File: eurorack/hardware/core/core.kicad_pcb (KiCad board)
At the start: 2 copper layers, 19.3 x 67.9 mm, 48 parts, among them J1 ConnNW, J2 ConnSW, J3 ConnNE, J4 ConnSE, J5 Power, J6 SWD, SW1 Reset, SW2 Boot0, U1 STM32F427VGT6, U2 TLV320AIC23BPW, U3 LM1117F-3.3, U4 LM4040C10IDBZR, Y1 Crystal

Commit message: Wire up power section
Signed-off-by: Petr Horacek <hrck@protonmail.com>
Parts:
- moved C4 27.0 mm to (169.0, 68.7), turned to 270 degrees
- moved Y1 24.6 mm to (164.4, 68.0)
- moved C1 21.0 mm to (159.4, 67.2), turned to 180 degrees
- moved C2 2.93 mm to (168.2, 46.2)
- moved C18 1.33 mm to (159.7, 72.7)
- moved C19 1.33 mm to (168.4, 72.4)
- moved C22 1.33 mm to (159.7, 80.3)
- moved C23 1.33 mm to (159.7, 76.3)
- moved R5 1.33 mm to (168.4, 76.2)
- moved R6 1.33 mm to (168.5, 74.3)
- moved U2 1.33 mm to (164.1, 76.5)
- moved R1 0.74 mm to (162.9, 47.1), turned to 180 degrees
- moved C16 0.42 mm to (165.6, 47.2)
- moved C3 0.41 mm to (159.4, 65.9)
- moved C10 0.32 mm to (169.1, 65.7)
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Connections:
- J1 pad 1: Net-(J1-Pad1) -> GND
- J1 pad 2: Net-(J1-Pad2) -> VCC
- J1 pad 3: Net-(J1-Pad3) -> VEE
- J1 pad 4: Net-(J1-Pad4) -> -10V
- J1 pad 5: Net-(J1-Pad5) -> +3V3
- J1 pad 6: Net-(J1-Pad6) -> +3.3VA
- J3 pad 1: Net-(J3-Pad1) -> GND
- J3 pad 2: Net-(J3-Pad2) -> VCC
- J3 pad 3: Net-(J3-Pad3) -> VEE
- J3 pad 4: Net-(J3-Pad4) -> -10V
- J3 pad 5: Net-(J3-Pad5) -> +3V3
- J3 pad 6: Net-(J3-Pad6) -> +3.3VA
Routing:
- net GND: track 0.00 -> 46.1 mm
- net +3V3: track 0.00 -> 32.0 mm
- net -10V: track 0.00 -> 29.8 mm
- net VEE: track 0.00 -> 26.4 mm
- net VCC: track 0.00 -> 23.9 mm
- net +3.3VA: track 0.00 -> 19.7 mm
- net Net-(C5-Pad1): track 0.00 -> 6.13 mm
- net Net-(FB1-Pad1): track 0.00 -> 5.69 mm
- net Net-(FB2-Pad1): track 0.00 -> 5.69 mm
- added copper zone on In1.Cu, net GND
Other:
- copper layers 2 -> 4
- board text added: "DSP"
- board text added: "Power"

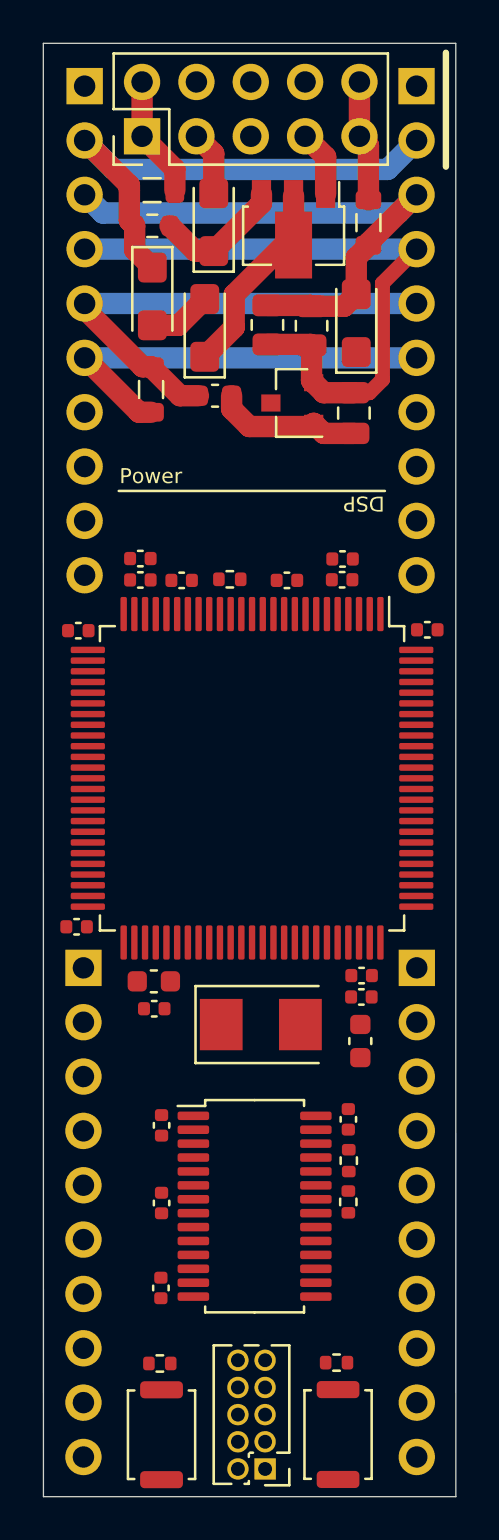
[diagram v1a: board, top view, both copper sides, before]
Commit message: Wire up DAC
Signed-off-by: Petr Horacek <hrck@protonmail.com>
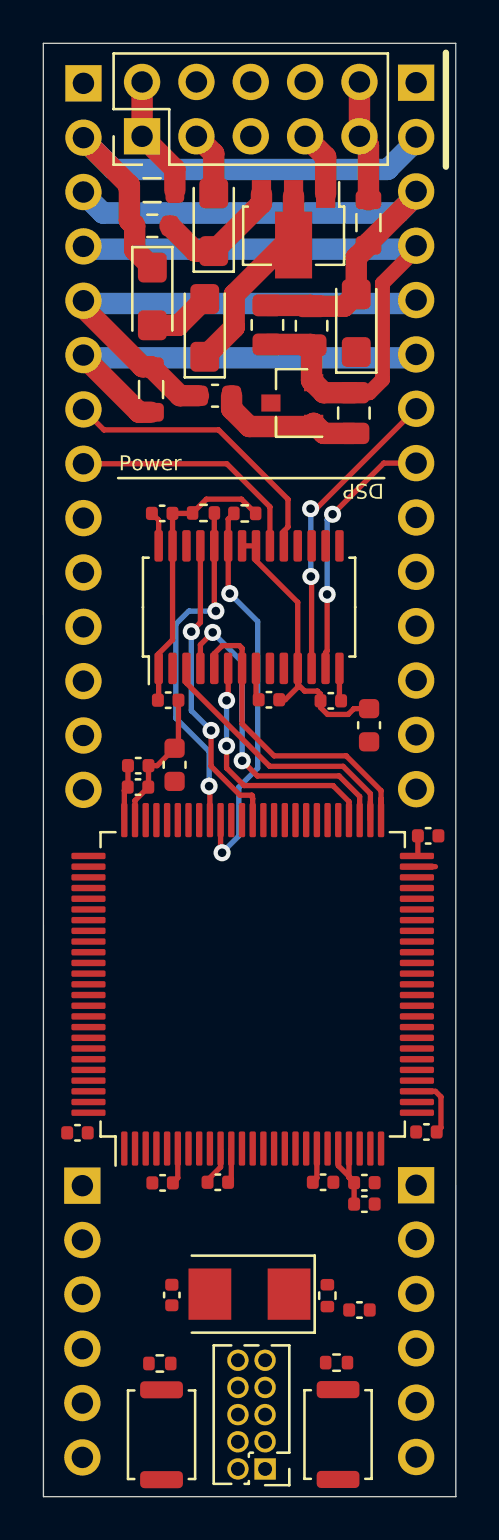
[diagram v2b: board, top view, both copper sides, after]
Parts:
- J1, J3: footprint Connector_PinHeader_2.54mm:PinHeader_1x10_P2.54mm_Vertical -> Connector_PinHeader_2.54mm:PinHeader_1x14_P2.54mm_Vertical
- J2, J4: footprint Connector_PinHeader_2.54mm:PinHeader_1x10_P2.54mm_Vertical -> Connector_PinHeader_2.54mm:PinHeader_1x06_P2.54mm_Vertical
- moved C2 35.3 mm to (160.2, 80.6), turned to 270 degrees
- moved R1 33.8 mm to (167.5, 80.6), turned to 90 degrees
- moved R5 32.5 mm to (163.6, 44.1), turned to 180 degrees
- moved C21 31.9 mm to (169.2, 76.3), turned to 0 degrees
- moved R6 31.0 mm to (161.7, 44.0), turned to 0 degrees
- moved C20 30.1 mm to (169.2, 75.3), turned to 0 degrees
- moved C19 29.6 mm to (159.8, 44.1), turned to 180 degrees
- moved C17 29.4 mm to (159.8, 75.4), turned to 180 degrees
- moved C15 28.9 mm to (167.3, 75.3), turned to 0 degrees
- moved C13 28.6 mm to (155.8, 73.0), turned to 180 degrees
- moved C22 28.6 mm to (167.6, 52.8), turned to 180 degrees
- moved C14 28.5 mm to (172.1, 73.0), turned to 180 degrees
- moved C16 28.3 mm to (162.3, 75.3), turned to 180 degrees
- moved U2 28.0 mm to (163.8, 48.5), turned to 90 degrees
- moved C23 24.0 mm to (164.7, 52.8), turned to 0 degrees
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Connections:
- J1 pad 7: Net-(J1-Pad7) -> RIN
- J1 pad 8: Net-(J1-Pad8) -> LIN
- J3 pad 7: Net-(J3-Pad7) -> LOUT
- J3 pad 8: Net-(J3-Pad8) -> ROUT
- U2 pad 12: Net-(U2-Pad12) -> LOUT
- U2 pad 13: Net-(U2-Pad13) -> ROUT
- U2 pad 19: Net-(U2-Pad19) -> RIN
- U2 pad 20: Net-(U2-Pad20) -> LIN
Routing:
- net +3V3: track 32.0 -> 57.1 mm
- net GND: track 46.1 -> 70.6 mm
- net I2C_SDA: track 0.00 -> 18.8 mm, vias 0 -> 2
- net I2C_SCL: track 0.00 -> 16.6 mm, vias 0 -> 2
- net I2S_WS: track 0.00 -> 15.9 mm
- net I2S_DIN: track 0.00 -> 15.8 mm, vias 0 -> 2
- net I2S_MCK: track 0.00 -> 14.5 mm, vias 0 -> 2
- net LOUT: track 0.00 -> 14.4 mm, vias 0 -> 2
- net RIN: track 0.00 -> 13.6 mm
- net I2S_CK: track 0.00 -> 13.5 mm
- net ROUT: track 0.00 -> 12.2 mm, vias 0 -> 2
- net I2S_DOUT: track 0.00 -> 11.9 mm, vias 0 -> 2
- net LIN: track 0.00 -> 11.4 mm
- net +3.3VA: track 19.7 -> 27.3 mm
- net Net-(C3-Pad1): track 0.00 -> 0.87 mm

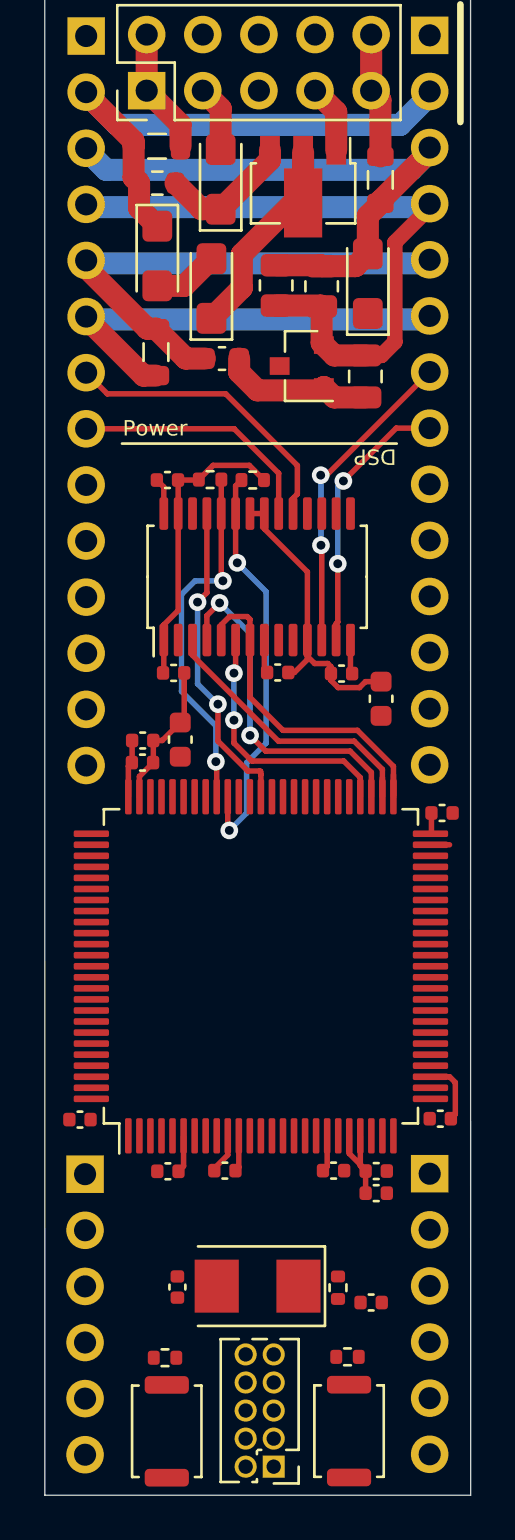
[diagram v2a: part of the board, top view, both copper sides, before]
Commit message: Wire up all pins
Signed-off-by: Petr Horacek <hrck@protonmail.com>
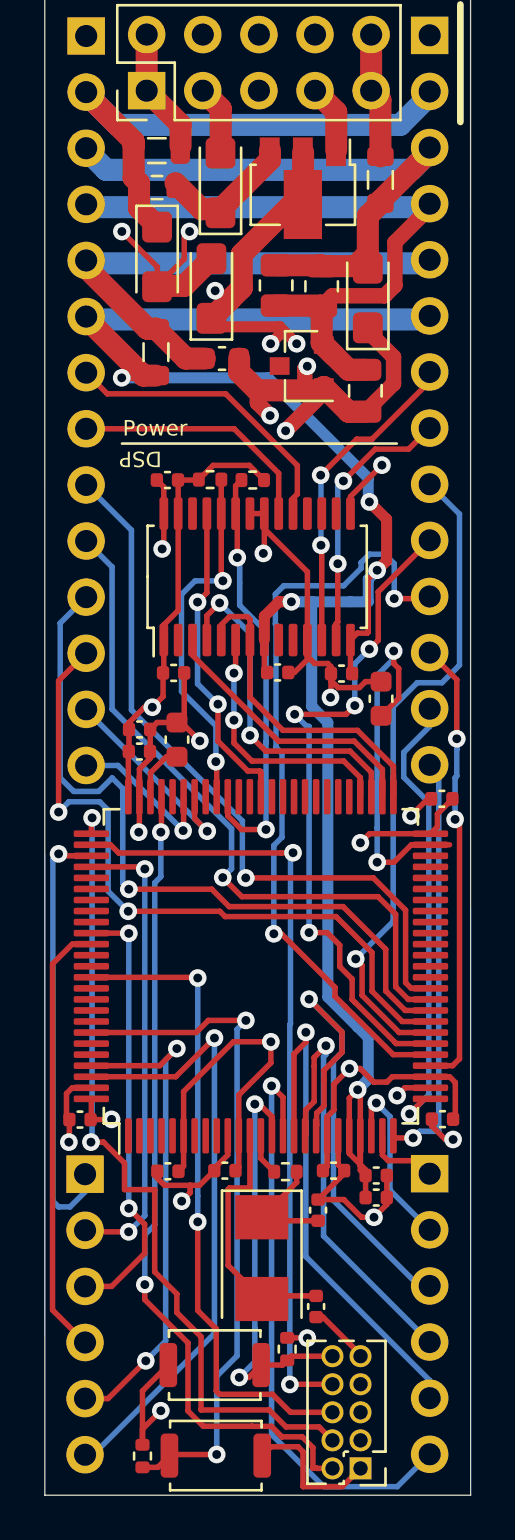
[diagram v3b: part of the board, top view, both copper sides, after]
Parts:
- moved SW1 6.78 mm to (161.9, 84.1), turned to 0 degrees
- moved C2 6.34 mm to (166.5, 81.5)
- moved R1 5.76 mm to (165.1, 75.4), turned to 0 degrees
- moved C1 4.82 mm to (166.6, 77.1), turned to 90 degrees
- moved R3 4.57 mm to (158.6, 88.2), turned to 90 degrees
- moved J6 3.93 mm to (168.5, 88.8)
- moved R2 2.75 mm to (165.2, 83.4), turned to 270 degrees
- moved SW2 2.48 mm to (161.9, 88.2), turned to 0 degrees
- moved Y1 1.28 mm to (164.0, 79.3), turned to 270 degrees
- moved C24 0.65 mm to (168.7, 40.0)
- moved C9 0.65 mm to (168.8, 35.8)
- moved C12 0.64 mm to (172.2, 58.5), turned to 180 degrees
- moved C10 0.52 mm to (158.5, 56.4)
- moved C11 0.52 mm to (158.5, 55.4)
- moved FB1 0.20 mm to (159.3, 29.2)
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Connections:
- J1 pad 10: Net-(J1-Pad10) -> PIN2
- J1 pad 11: Net-(J1-Pad11) -> PIN3
- J1 pad 12: Net-(J1-Pad12) -> PIN4
- J1 pad 13: Net-(J1-Pad13) -> PIN5
- J1 pad 14: Net-(J1-Pad14) -> PIN6
- J1 pad 9: Net-(J1-Pad9) -> PIN1
- J2 pad 1: Net-(J2-Pad1) -> PIN7
- J2 pad 2: Net-(J2-Pad2) -> PIN8
- J2 pad 3: Net-(J2-Pad3) -> PIN9
- J2 pad 4: Net-(J2-Pad4) -> PIN10
- J2 pad 5: Net-(J2-Pad5) -> PIN11
- J2 pad 6: Net-(J2-Pad6) -> PIN12
- J3 pad 10: Net-(J3-Pad10) -> PIN14
- J3 pad 11: Net-(J3-Pad11) -> PIN15
- J3 pad 12: Net-(J3-Pad12) -> PIN16
- J3 pad 13: Net-(J3-Pad13) -> PIN17
- J3 pad 14: Net-(J3-Pad14) -> PIN18
- J3 pad 9: Net-(J3-Pad9) -> PIN13
- J4 pad 1: Net-(J4-Pad1) -> PIN19
- J4 pad 2: Net-(J4-Pad2) -> PIN20
- J4 pad 3: Net-(J4-Pad3) -> PIN21
- J4 pad 4: Net-(J4-Pad4) -> PIN22
- J4 pad 5: Net-(J4-Pad5) -> PIN23
- J4 pad 6: Net-(J4-Pad6) -> PIN24
- U1 pad 15: Net-(U1-Pad15) -> PIN24
- U1 pad 16: Net-(U1-Pad16) -> PIN23
- U1 pad 17: Net-(U1-Pad17) -> PIN22
- U1 pad 18: Net-(U1-Pad18) -> PIN21
- U1 pad 23: Net-(U1-Pad23) -> PIN20
- U1 pad 24: Net-(U1-Pad24) -> PIN19
- U1 pad 25: Net-(U1-Pad25) -> PIN18
- U1 pad 26: Net-(U1-Pad26) -> PIN17
- U1 pad 29: Net-(U1-Pad29) -> PIN16
- U1 pad 30: Net-(U1-Pad30) -> PIN15
- U1 pad 31: Net-(U1-Pad31) -> PIN14
- U1 pad 32: Net-(U1-Pad32) -> PIN13
- U1 pad 33: Net-(U1-Pad33) -> PIN4
- U1 pad 34: Net-(U1-Pad34) -> PIN3
- U1 pad 35: Net-(U1-Pad35) -> PIN2
- U1 pad 36: Net-(U1-Pad36) -> PIN1
- U1 pad 69: Net-(U1-Pad69) -> PIN5
- U1 pad 70: Net-(U1-Pad70) -> PIN6
- U1 pad 78: Net-(U1-Pad78) -> PIN7
- U1 pad 79: Net-(U1-Pad79) -> PIN8
- U1 pad 85: Net-(U1-Pad85) -> PIN9
- U1 pad 86: Net-(U1-Pad86) -> PIN10
- U1 pad 97: Net-(U1-Pad97) -> PIN11
- U1 pad 98: Net-(U1-Pad98) -> PIN12
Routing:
- net +3.3VA: track 27.3 -> 88.1 mm, vias 0 -> 5
- net GND: track 70.6 -> 127.9 mm, vias 0 -> 18
- net +3V3: track 57.1 -> 100.5 mm, vias 0 -> 9
- net JTCK: track 0.00 -> 37.3 mm, vias 0 -> 2
- net JTMS: track 0.00 -> 37.1 mm, vias 0 -> 2
- net JTDI: track 0.00 -> 35.4 mm, vias 0 -> 2
- net PIN15: track 0.00 -> 34.9 mm, vias 0 -> 2
- net PIN3: track 0.00 -> 33.9 mm, vias 0 -> 1
- net PIN1: track 0.00 -> 33.4 mm, vias 0 -> 1
- net PIN4: track 0.00 -> 32.0 mm, vias 0 -> 2
- net PIN2: track 0.00 -> 31.7 mm, vias 0 -> 1
- net BOOT0: track 0.00 -> 31.1 mm, vias 0 -> 2
- net PIN14: track 0.00 -> 30.7 mm, vias 0 -> 4
- net PIN13: track 0.00 -> 30.2 mm, vias 0 -> 1
- net JTDO: track 0.00 -> 29.5 mm, vias 0 -> 2
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- added copper zone on In2.Cu, net +3V3

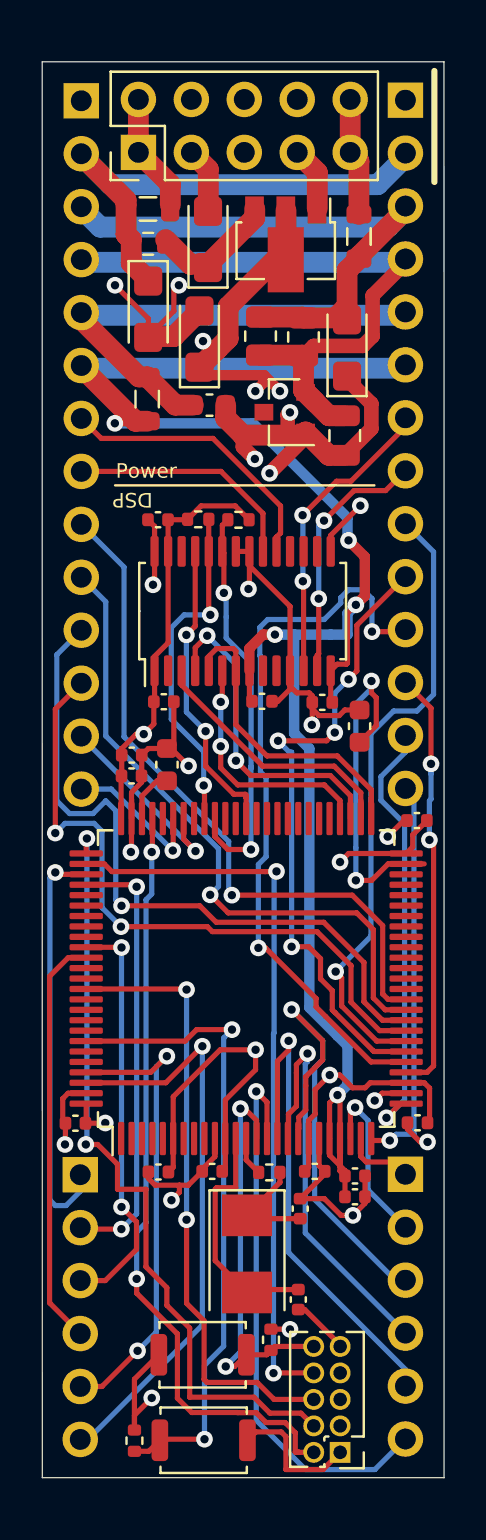
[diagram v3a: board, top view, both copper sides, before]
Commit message: Refill ground and power planes
Signed-off-by: Petr Horacek <hrck@protonmail.com>
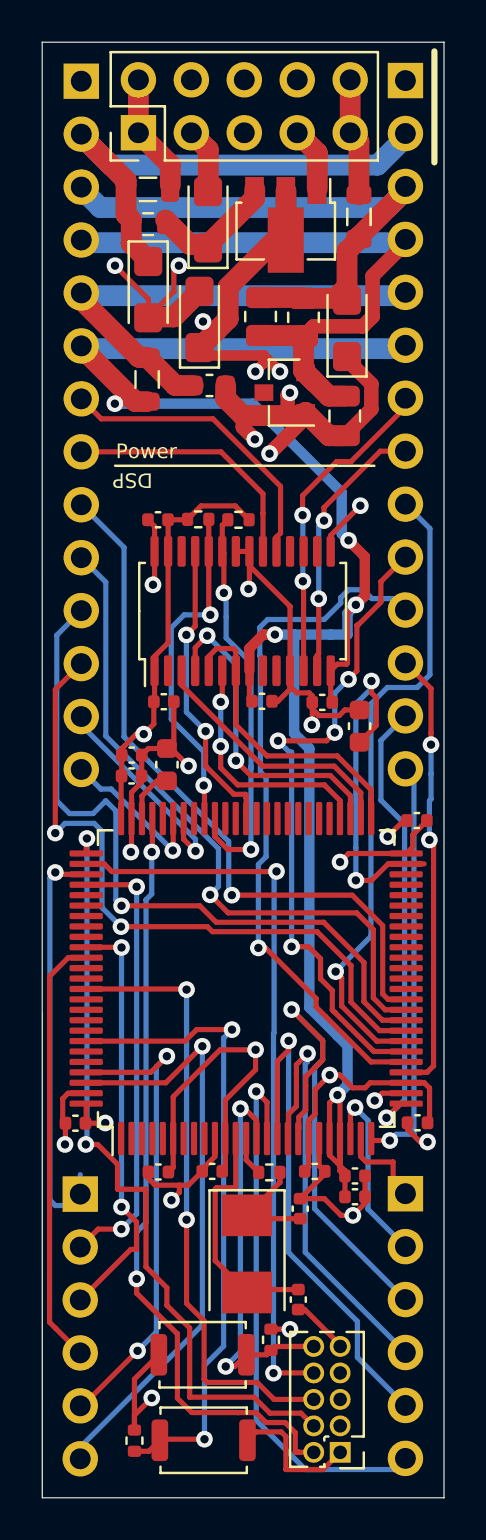
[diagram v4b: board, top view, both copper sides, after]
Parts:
- moved C5 0.94 mm to (162.2, 29.7)
- moved FB1 0.94 mm to (159.3, 28.2)
- moved FB2 0.94 mm to (169.4, 29.5)
- moved J3 0.94 mm to (171.6, 23.0)
- moved J5 0.94 mm to (158.8, 25.5)
- moved C24 0.94 mm to (168.7, 39.1)
- moved C6 0.94 mm to (161.7, 34.5)
- moved C7 0.94 mm to (162.2, 37.6)
- moved C8 0.94 mm to (159.3, 33.0)
- moved C9 0.94 mm to (168.8, 34.9)
- moved FB3 0.94 mm to (159.2, 37.3)
- moved J1 0.94 mm to (156.1, 23.0)
- moved R4 0.94 mm to (159.3, 29.9)
- moved R7 0.94 mm to (164.7, 34.3)
- moved R8 0.94 mm to (166.7, 34.4)
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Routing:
- net GND: track 127.9 -> 131.8 mm
- net PIN17: track 20.9 -> 23.2 mm
- net PIN15: track 34.9 -> 33.5 mm, vias 2 -> 1
- net +3.3VA: track 88.1 -> 89.1 mm
- net PIN13: track 30.2 -> 31.2 mm
- net PIN14: track 30.7 -> 31.6 mm
- net PIN5: track 9.58 -> 10.5 mm
- net PIN4: track 32.0 -> 33.0 mm
- net PIN3: track 33.9 -> 34.8 mm
- net PIN2: track 31.7 -> 32.7 mm
- net LOUT: track 14.9 -> 15.8 mm
- net RIN: track 13.6 -> 14.5 mm
- net PIN18: track 19.0 -> 19.9 mm
- net PIN1: track 33.4 -> 34.4 mm
- net LIN: track 11.4 -> 12.3 mm
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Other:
- board size 19.3 x 67.9 mm -> 19.3 x 69.8 mm

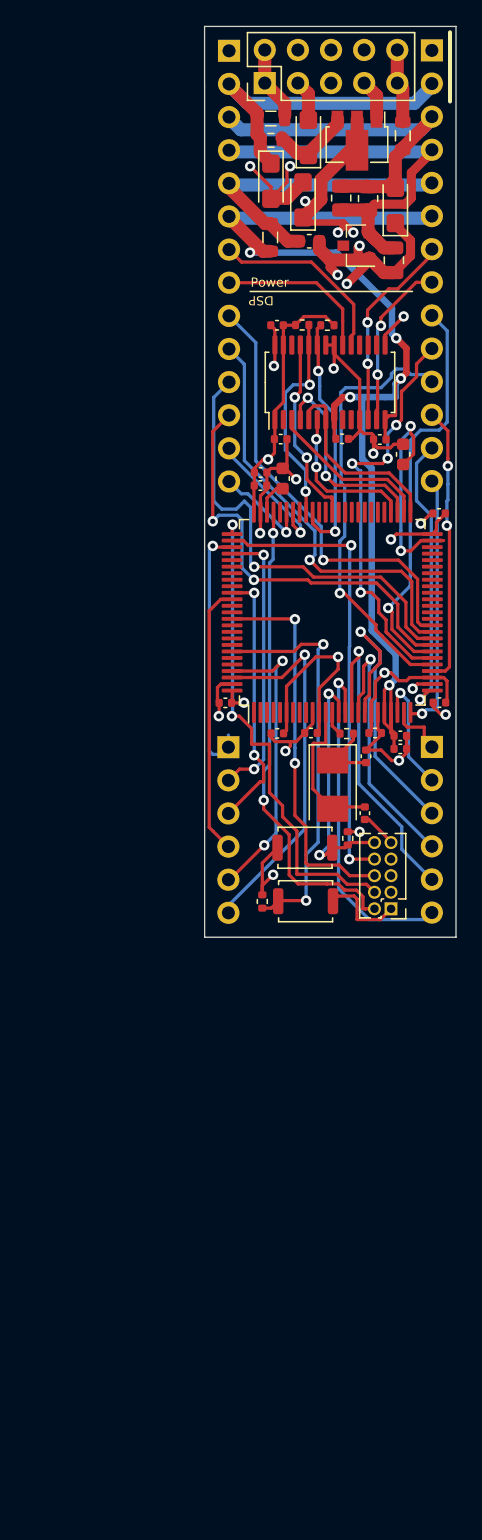
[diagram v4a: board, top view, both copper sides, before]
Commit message: Add labels
Signed-off-by: Petr Horacek <hrck@protonmail.com>
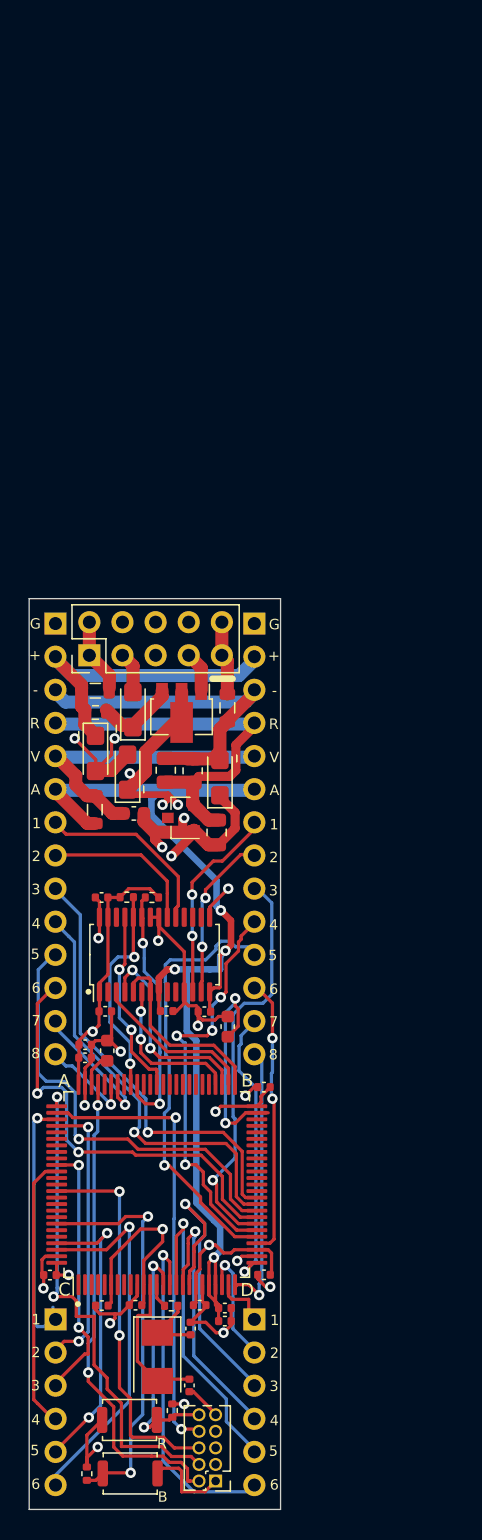
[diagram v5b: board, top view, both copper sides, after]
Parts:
- moved J3 46.0 mm to (158.0, 66.9)
- moved C12 46.0 mm to (158.7, 102.5)
- moved J4 46.0 mm to (158.0, 120.3)
- moved C24 45.9 mm to (155.1, 83.0)
- moved C11 45.9 mm to (145.0, 99.2)
- moved C15 45.9 mm to (153.8, 119.2)
- moved C17 45.9 mm to (146.3, 119.2)
- moved C23 45.9 mm to (151.3, 96.7)
- moved FB1 45.9 mm to (145.8, 72.1)
- moved J6 45.9 mm to (155.0, 132.7)
- moved R1 45.9 mm to (151.6, 119.2)
- moved R3 45.9 mm to (145.2, 132.1)
- moved R6 45.9 mm to (148.2, 87.9)
- moved U4 45.9 mm to (152.4, 81.8)
- moved C10 45.9 mm to (145.0, 100.2)
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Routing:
- net GND: track 131.8 -> 158.3 mm
- net +3.3VA: track 89.1 -> 84.6 mm, vias 5 -> 4
- net PIN18: track 19.9 -> 21.1 mm
- net PIN3: track 34.8 -> 33.8 mm
- net PIN17: track 23.2 -> 22.2 mm
- net +3V3: track 100.5 -> 101.3 mm
- net JTCK: track 37.3 -> 38.0 mm
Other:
- board text added: "+"
- board text added: "-"
- board text added: "1"
- board text added: "2"
- board text added: "3"
- board text added: "4"
- board text added: "5"
- board text added: "6"
- board text added: "7"
- board text added: "8"
- board text added: "A"
- board text added: "B"
- board text added: "C"
- board text added: "D"
- board text added: "G"
- board text added: "R"
- board text added: "V"
- board text removed: "DSP"
- board text removed: "Power"
